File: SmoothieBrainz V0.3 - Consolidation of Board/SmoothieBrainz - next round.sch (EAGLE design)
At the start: 125 parts, among them IC1 LPC1769, IC5 LD117ADT33TR, Q1 BSL207SP, Q2 12MHz, SW1 SW_TACT_4P_B, SW3 SW_TACT_4P_B, U2 HC_05, U3 USD-SOCKETUSD, X14 USBPTH

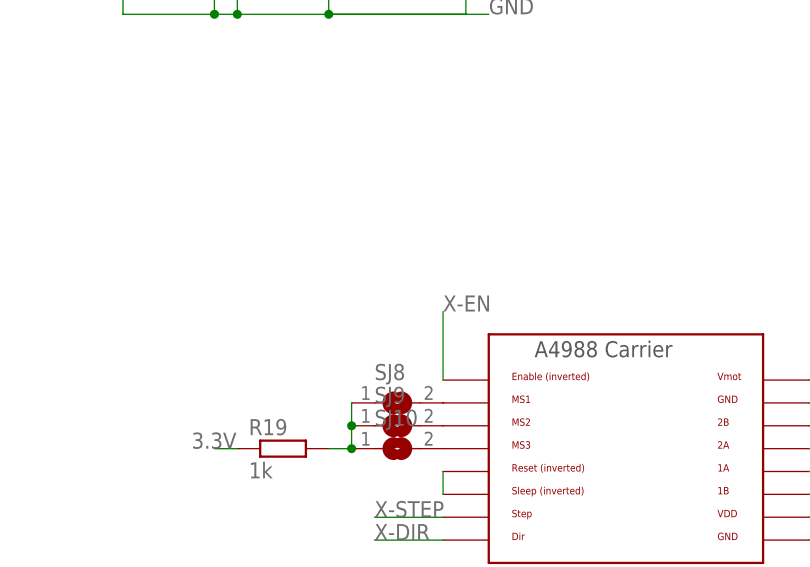
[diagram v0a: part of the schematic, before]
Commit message: More trace ripup.  About to change motor 1 traces
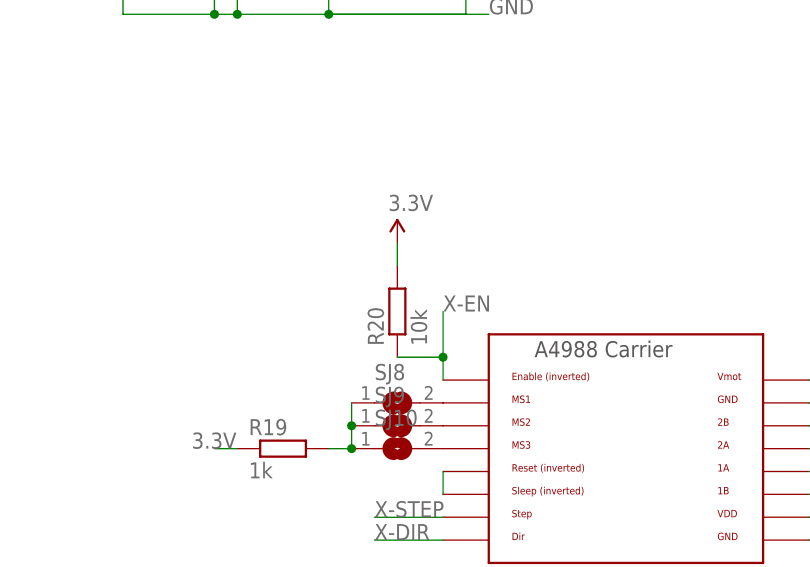
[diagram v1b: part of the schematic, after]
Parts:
- added R20: 10k, resistor:R-EU_R0603
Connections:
- net 3.3V: now also R20.2
- net X-EN: now also R20.1
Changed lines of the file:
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@@
 <part name="SJ9" library="jumper" deviceset="SJ" device=""/>
 <part name="SJ10" library="jumper" deviceset="SJ" device=""/>
+<part name="R20" library="resistor" deviceset="R-EU_" device="R0603" value="10k"/>
+<part name="P+5" library="SparkFun" deviceset="3.3V" device=""/>
 </parts>
 <sheets>
@@
 <instance part="SJ9" gate="1" x="317.5" y="264.16"/>
 <instance part="SJ10" gate="1" x="317.5" y="261.62"/>
+<instance part="R20" gate="G$1" x="317.5" y="276.86" rot="R90"/>
+<instance part="P+5" gate="G$1" x="317.5" y="284.48"/>
 </instances>
 <busses>
@@
 <label x="294.64" y="261.62" size="1.778" layer="95"/>
 </segment>
+<segment>
+<pinref part="R20" gate="G$1" pin="2"/>
+<pinref part="P+5" gate="G$1" pin="3.3V"/>
+<wire x1="317.5" y1="281.94" x2="317.5" y2="284.48" width="0.1524" layer="91"/>
+</segment>
 </net>
 <net name="AVCC" class="0">
@@
 <segment>
 <pinref part="U$1" gate="G$1" pin="EN"/>
-<wire x1="322.58" y1="269.24" x2="322.58" y2="276.86" width="0.1524" layer="91"/>
+<wire x1="322.58" y1="269.24" x2="322.58" y2="271.78" width="0.1524" layer="91"/>
 <label x="322.58" y="276.86" size="1.778" layer="95"/>
-</segment>
-</net>
+<pinref part="R20" gate="G$1" pin="1"/>
+<wire x1="322.58" y1="271.78" x2="322.58" y2="276.86" width="0.1524" layer="91"/>
+<wire x1="317.5" y1="271.78" x2="322.58" y2="271.78" width="0.1524" layer="91"/>
+<junction x="322.58" y="271.78"/>
+</segment>
+</net>

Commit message: 2 templates for stepper driver completed
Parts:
- added C32, C33: 104, resistor:C-EUC0603
- added C34: 100uF, resistor:CPOL-EU153CLV-0605
- added R25: 1k, resistor:R-EU_R0603
- added R26: 10k, resistor:R-EU_R0603
- added SJ11, SJ12, SJ13: (no value), jumper:SJ
- C29, C30: value 100nF -> 104
- D12: value (none) -> M4
- JP2: device pinhead:PINHD-1X30 -> SparkFun-Connectors:M04POLAR_LOCK
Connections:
- removed net X-DIR: U$1.DIR
- removed net X-EN: R20.1, U$1.EN
- removed net X-STEP: U$1.STEP
- new net 1A2M: JP2.2, U$5.1A
- new net 1B2M: JP2.1, U$5.1B
- new net 2A2M: JP2.3, U$5.2A
- new net 2B2M: JP2.4, U$5.2B
- new net N$12: U$5.RST, U$5.SLEEP
- new net N$14: R25.2, SJ11.1, SJ12.1, SJ13.1
- new net N$15: SJ11.2, U$5.MS1
- new net N$17: SJ12.2, U$5.MS2
- new net N$19: SJ13.2, U$5.MS3
- net 24V: now also C32.1, C34.+, U$5.VMOT; no longer JP2.25, JP2.26
- net 3.3V: now also C33.1, R25.1, R26.2, U$5.VDD
- net 5VREG: no longer JP2.27
- net DIR1: now also U$1.DIR; no longer JP2.5
- net DIR2: now also U$5.DIR; no longer JP2.8
- net DIR3: no longer JP2.11
- net DIR4: no longer JP2.14
- net DIR5: no longer JP2.17
- net EN1: now also R20.1, U$1.EN; no longer JP2.4
- net EN2: now also R26.1, U$5.EN; no longer JP2.7
- net EN3: no longer JP2.10
- net EN4: no longer JP2.13
- net EN5: no longer JP2.16
- net GND: now also C32.2, C33.2, C34.-, U$5.GND@0, U$5.GND@1; no longer JP2.28, JP2.29, JP2.30
- net P1_22-3RD-SMALL-FET: no longer JP2.20
- net P1_23-3RD-LARGE-FET: no longer JP2.19
- net P2.6_FAN_FET: no longer JP2.23
- net P2.7_HOTEND_FET: no longer JP2.24
- net PWM0_PSU_OUT: no longer JP2.21
- net PWM1_BED_HEATER: no longer JP2.22
- net SD_MISO: no longer JP2.2
- net SD_MOSI: no longer JP2.3
- net SD_SCK: no longer JP2.1
- net STP1: now also U$1.STEP; no longer JP2.6
- net STP2: now also U$5.STEP; no longer JP2.9
- net STP3: no longer JP2.12
- net STP4: no longer JP2.15
- net STP5: no longer JP2.18

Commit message: Lots of voltage rails and pours
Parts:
- added C35, C36: 104, resistor:C-EUC0603
- added C37: 100uF, resistor:CPOL-EU153CLV-0605
- added JP7: (no value), SparkFun-Connectors:M04POLAR_LOCK
- added LED6: (no value), adafruit:LEDCHIPLED_0805
- added R27: 10r, adafruit:R-US_R0603
- added R30: 100k, adafruit:R-US_R0603
- added R32: 1k, adafruit:R-US_R0603
- added R33: 1k, resistor:R-EU_R0603
- added R34: 10k, resistor:R-EU_R0603
- added SJ14, SJ15, SJ16: (no value), jumper:SJ
- added U$10: SUM120N04-1M7L-GE3, Cohesion_parts:N-POWER-MOSFETD2PAK-MOSFET
- added X1: GMSTBV2, con-phoenix-762:GMSTBV2
- added X2: MSTBA2, con-phoenix-508:MSTBA2
- added X3: MSTBA4, con-phoenix-508:MSTBA4
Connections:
- new net +12VHEATBED: R32.1
- new net 1A3M: JP7.2, U$6.1A
- new net 1B3M: JP7.1, U$6.1B
- new net 2A3M: JP7.3, U$6.2A
- new net 2B3M: JP7.4, U$6.2B
- new net D11: R27.1, R30.2
- new net HEATBED-CONTROL: LED6.C, U$10.D, X3-4.1
- new net HEATBEDVIN: X3-1.1, X3-3.1
- new net N$20: R27.2, U$10.G
- new net N$21: LED6.A, R32.2
- new net N$22: U$6.RST, U$6.SLEEP
- new net N$24: R33.2, SJ14.1, SJ15.1, SJ16.1
- new net N$25: SJ14.2, U$6.MS1
- new net N$26: SJ15.2, U$6.MS2
- new net N$27: SJ16.2, U$6.MS3
- net 24V: now also C35.1, C37.+, U$6.VMOT, X2-1.1
- net 3.3V: now also C36.1, R33.1, R34.2, U$6.VDD
- net 5V: now also XMN.1, XMX.1, YMN.1, YMX.1, ZMN.1, ZMX.1
- net 5VREG: no longer XMN.1, XMX.1, YMN.1, YMX.1, ZMN.1, ZMX.1
- net DIR3: now also U$6.DIR
- net EN3: now also R34.1, U$6.EN
- net GND: now also C35.2, C36.2, C37.-, R30.1, U$10.S, U$6.GND@0, U$6.GND@1, X2-2.1, X3-2.1
- net STP3: now also U$6.STEP

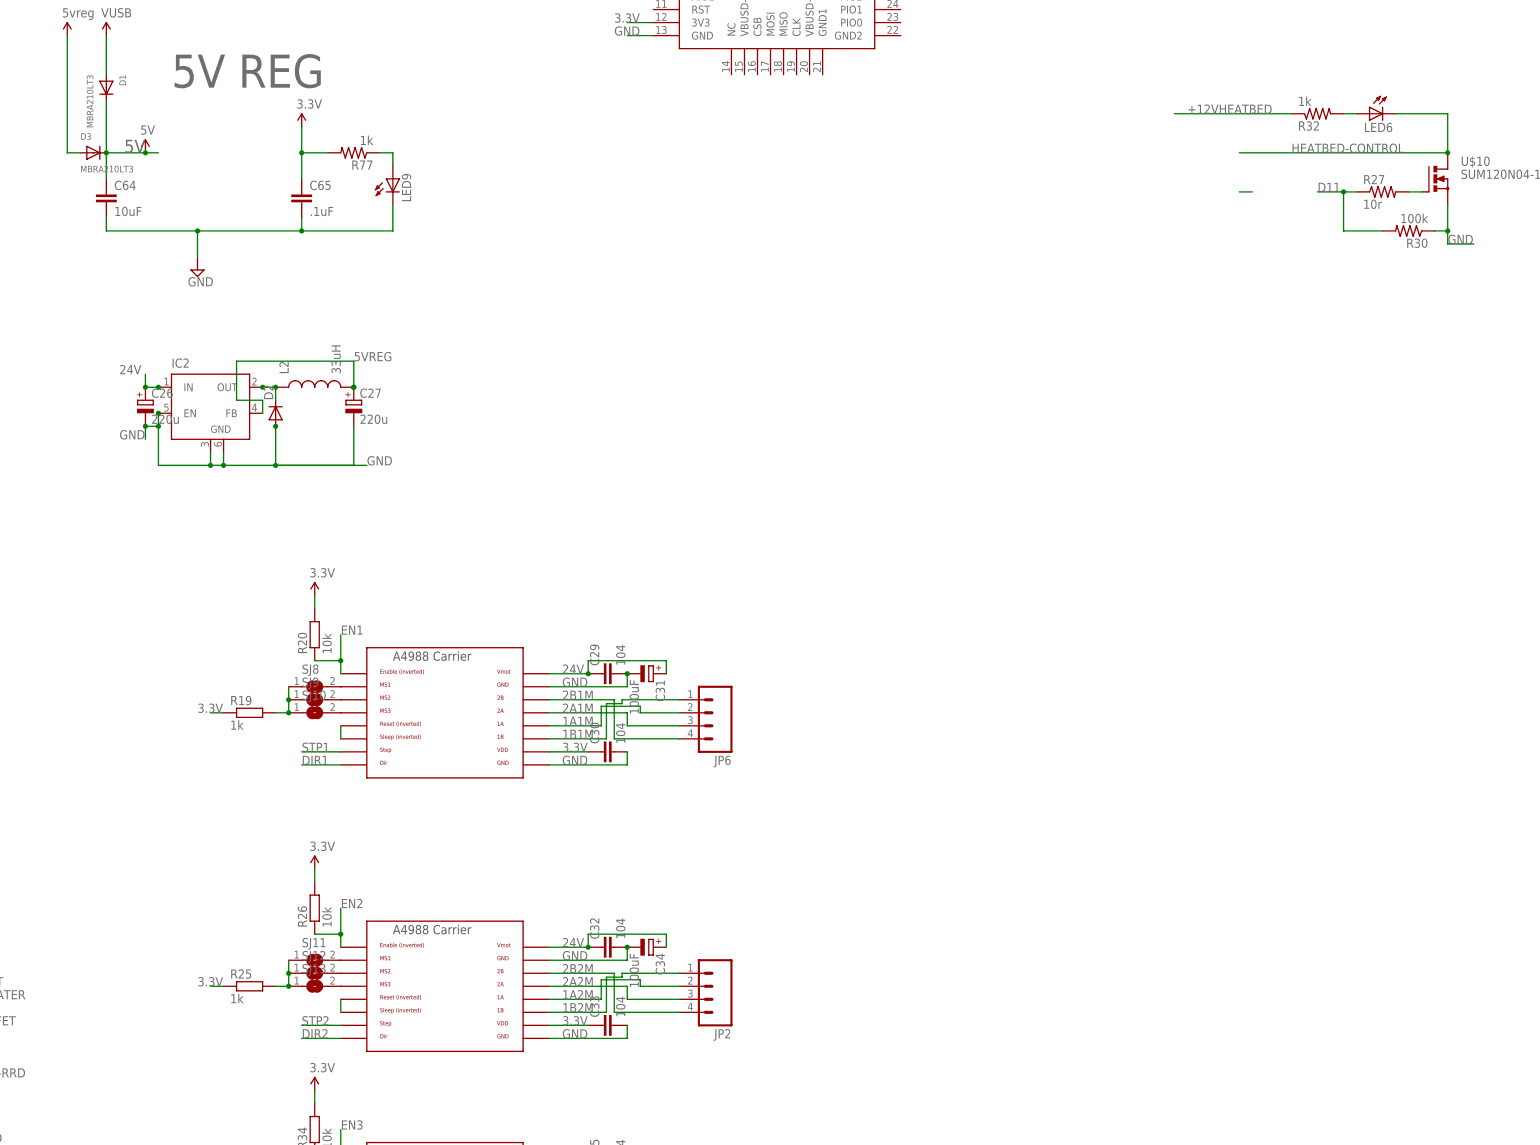
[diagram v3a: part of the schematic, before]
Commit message: heatbed mosfet/ motor driver changes
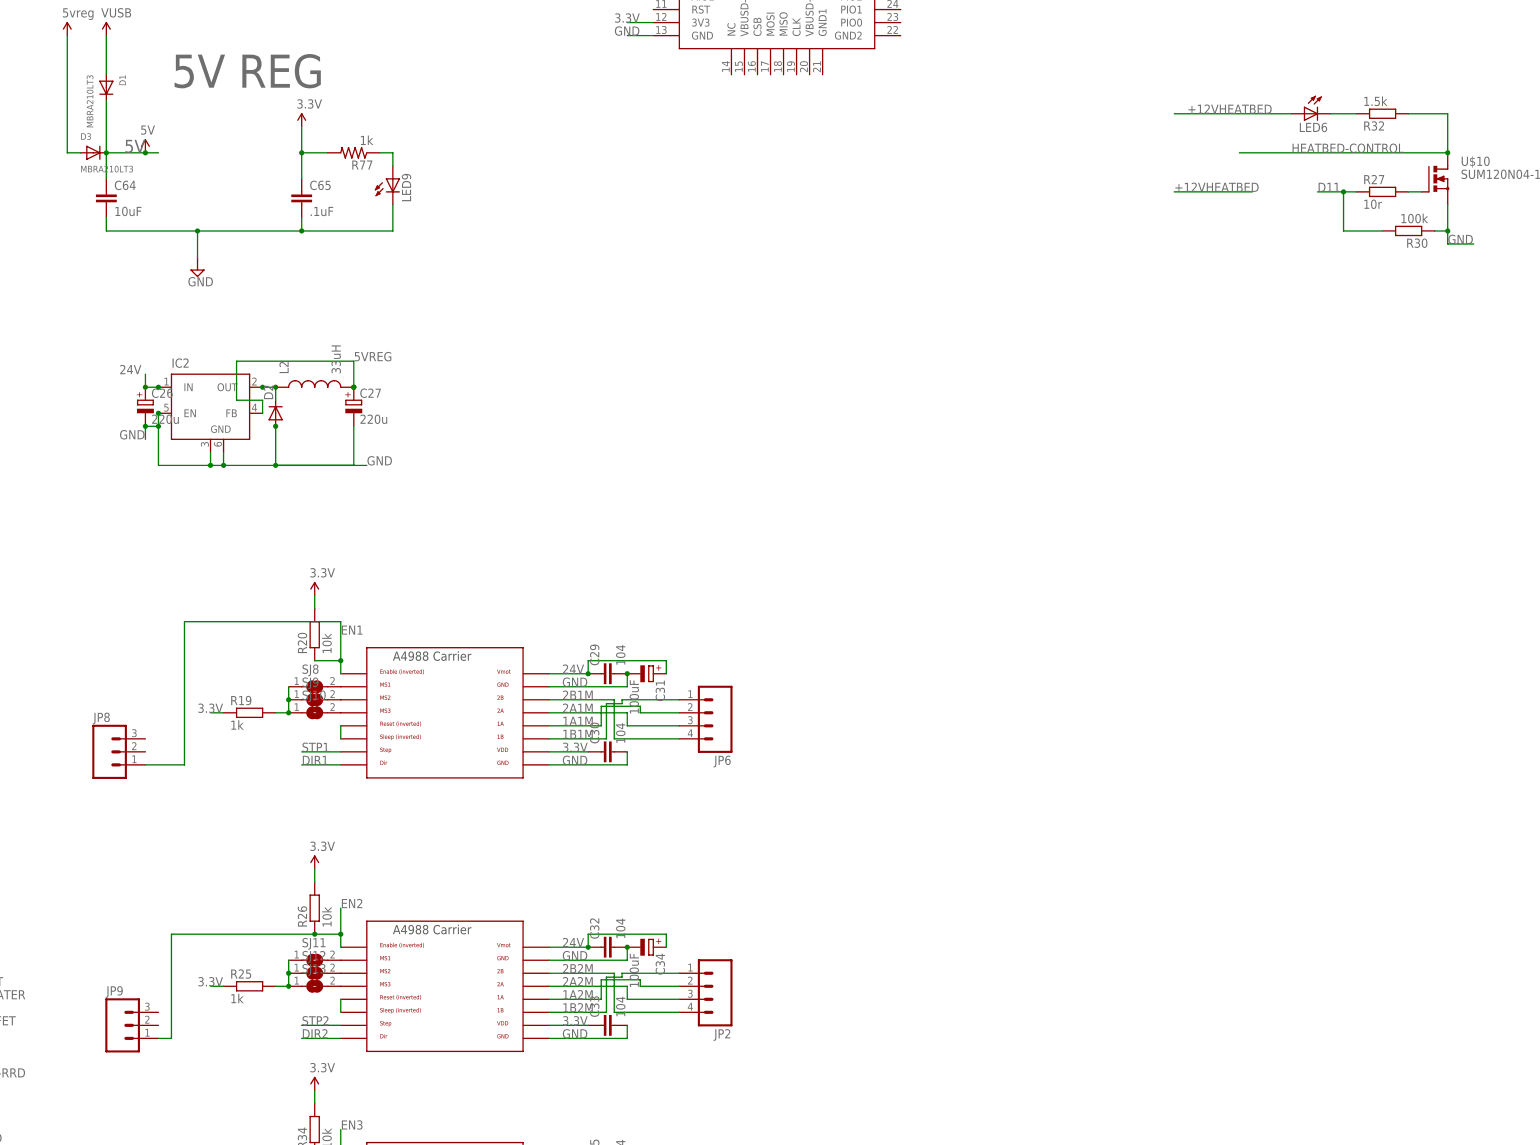
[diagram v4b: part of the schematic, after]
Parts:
- added JP8, JP9: (no value), SparkFun-Connectors:M03LOCK
- LED6: device adafruit:LEDCHIPLED_0805 -> led:LEDSML0805
- R27, R30: device adafruit:R-US_R0603 -> resistor:R-EU_R0603
- R32: value 1k -> 1.5k; device adafruit:R-US_R0603 -> resistor:R-EU_R0603
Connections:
- net +12VHEATBED: now also LED6.A; no longer R32.1
- net EN1: now also JP8.1
- net EN2: now also JP9.1
- net HEATBED-CONTROL: now also R32.2; no longer LED6.C
- net N$21: now also LED6.C, R32.1; no longer LED6.A, R32.2
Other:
- moved on the sheet: LED6
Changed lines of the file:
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@@
 <part name="X1" library="con-phoenix-762" deviceset="GMSTBV2" device=""/>
 <part name="U$10" library="Cohesion_parts" deviceset="N-POWER-MOSFET" device="D2PAK-MOSFET" value="SUM120N04-1M7L-GE3"/>
-<part name="R27" library="adafruit" deviceset="R-US_" device="R0603" value="10r"/>
-<part name="R30" library="adafruit" deviceset="R-US_" device="R0603" value="100k"/>
-<part name="R32" library="adafruit" deviceset="R-US_" device="R0603" value="1k"/>
-<part name="LED6" library="adafruit" deviceset="LED" device="CHIPLED_0805"/>
+<part name="R27" library="resistor" deviceset="R-EU_" device="R0603" value="10r"/>
+<part name="R30" library="resistor" deviceset="R-EU_" device="R0603" value="100k"/>
+<part name="R32" library="resistor" deviceset="R-EU_" device="R0603" value="1.5k"/>
+<part name="LED6" library="led" deviceset="LED" device="SML0805"/>
 <part name="X2" library="con-phoenix-508" deviceset="MSTBA2" device=""/>
 <part name="X3" library="con-phoenix-508" deviceset="MSTBA4" device=""/>
@@
 <part name="R34" library="resistor" deviceset="R-EU_" device="R0603" value="10k"/>
 <part name="P+7" library="SparkFun" deviceset="3.3V" device=""/>
+<part name="JP8" library="SparkFun-Connectors" deviceset="M03" device="LOCK"/>
+<part name="JP9" library="SparkFun-Connectors" deviceset="M03" device="LOCK"/>
 </parts>
 <sheets>
@@
 <instance part="R27" gate="G$1" x="525.78" y="363.22"/>
 <instance part="R30" gate="G$1" x="530.86" y="355.6" rot="R180"/>
-<instance part="R32" gate="G$1" x="513.08" y="378.46" rot="MR180"/>
-<instance part="LED6" gate="G$1" x="523.24" y="378.46" rot="MR270"/>
+<instance part="R32" gate="G$1" x="525.78" y="378.46" rot="MR180"/>
+<instance part="LED6" gate="G$1" x="510.54" y="378.46" rot="MR270"/>
 <instance part="X2" gate="-1" x="71.12" y="307.34"/>
 <instance part="X2" gate="-2" x="71.12" y="302.26"/>
@@
 <instance part="R34" gate="G$1" x="317.5" y="180.34" rot="R90"/>
 <instance part="P+7" gate="G$1" x="317.5" y="187.96"/>
+<instance part="JP8" gate="G$1" x="276.86" y="254"/>
+<instance part="JP9" gate="G$1" x="279.4" y="200.66"/>
 </instances>
 <busses>
@@
 <label x="322.58" y="276.86" size="1.778" layer="95"/>
 <pinref part="R20" gate="G$1" pin="1"/>
-<wire x1="322.58" y1="271.78" x2="322.58" y2="276.86" width="0.1524" layer="91"/>
+<wire x1="322.58" y1="271.78" x2="322.58" y2="279.4" width="0.1524" layer="91"/>
 <wire x1="317.5" y1="271.78" x2="322.58" y2="271.78" width="0.1524" layer="91"/>
 <junction x="322.58" y="271.78"/>
+<pinref part="JP8" gate="G$1" pin="1"/>
+<wire x1="284.48" y1="251.46" x2="292.1" y2="251.46" width="0.1524" layer="91"/>
+<wire x1="292.1" y1="251.46" x2="292.1" y2="279.4" width="0.1524" layer="91"/>
+<wire x1="292.1" y1="279.4" x2="322.58" y2="279.4" width="0.1524" layer="91"/>
 </segment>
 </net>
@@
 <wire x1="317.5" y1="218.44" x2="322.58" y2="218.44" width="0.1524" layer="91"/>
 <junction x="322.58" y="218.44"/>
+<pinref part="JP9" gate="G$1" pin="1"/>
+<wire x1="287.02" y1="198.12" x2="289.56" y2="198.12" width="0.1524" layer="91"/>
+<wire x1="289.56" y1="198.12" x2="289.56" y2="218.44" width="0.1524" layer="91"/>
+<wire x1="289.56" y1="218.44" x2="317.5" y2="218.44" width="0.1524" layer="91"/>
+<junction x="317.5" y="218.44"/>
 </segment>
 </net>
@@
 <net name="+12VHEATBED" class="4">
 <segment>
-<wire x1="500.38" y1="363.22" x2="497.84" y2="363.22" width="0.1524" layer="91"/>
+<wire x1="500.38" y1="363.22" x2="485.14" y2="363.22" width="0.1524" layer="91"/>
+<label x="485.14" y="363.22" size="1.778" layer="95"/>
 </segment>
 <segment>
-<pinref part="R32" gate="G$1" pin="1"/>
-<wire x1="508" y1="378.46" x2="485.14" y2="378.46" width="0.1524" layer="91"/>
 <label x="487.68" y="378.46" size="1.778" layer="95"/>
+<pinref part="LED6" gate="G$1" pin="A"/>
+<wire x1="508" y1="378.46" x2="485.14" y2="378.46" width="0.1524" layer="91"/>
 </segment>
 </net>
@@
 <wire x1="497.84" y1="370.84" x2="538.48" y2="370.84" width="0.1524" layer="91"/>
 <label x="508" y="370.84" size="1.778" layer="95"/>
-<pinref part="LED6" gate="G$1" pin="C"/>
-<wire x1="528.32" y1="378.46" x2="538.48" y2="378.46" width="0.1524" layer="91"/>
 <wire x1="538.48" y1="378.46" x2="538.48" y2="370.84" width="0.1524" layer="91"/>
 <junction x="538.48" y="370.84"/>
+<pinref part="R32" gate="G$1" pin="2"/>
+<wire x1="530.86" y1="378.46" x2="538.48" y2="378.46" width="0.1524" layer="91"/>
 </segment>
 <segment>
@@
 </segment>
 </net>
-<net name="N$21" class="0">
-<segment>
-<pinref part="R32" gate="G$1" pin="2"/>
-<pinref part="LED6" gate="G$1" pin="A"/>
-<wire x1="518.16" y1="378.46" x2="520.7" y2="378.46" width="0.1524" layer="91"/>
-</segment>
-</net>
 <net name="N$22" class="0">
 <segment>
@@
 </segment>
 </net>
+<net name="N$21" class="0">
+<segment>
+<pinref part="LED6" gate="G$1" pin="C"/>
+<pinref part="R32" gate="G$1" pin="1"/>
+<wire x1="515.62" y1="378.46" x2="520.7" y2="378.46" width="0.1524" layer="91"/>
+</segment>
+</net>
